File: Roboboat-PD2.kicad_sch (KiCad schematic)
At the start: 36 parts, among them J1 12V, J10 Motor, J11 Motor, J12 Motor, J13 Motor, J14 5V, J15 14.4V, J17 PGOOD TP, J18 GND TP, J19 PGOOD, J2 Bucky, J3 Jetson, J4 Motor, J5 Motor, J6 Motor, J7 Motor, J8 Motor, J9 Motor, SW1 Jumper, U1 AOZ2379QI

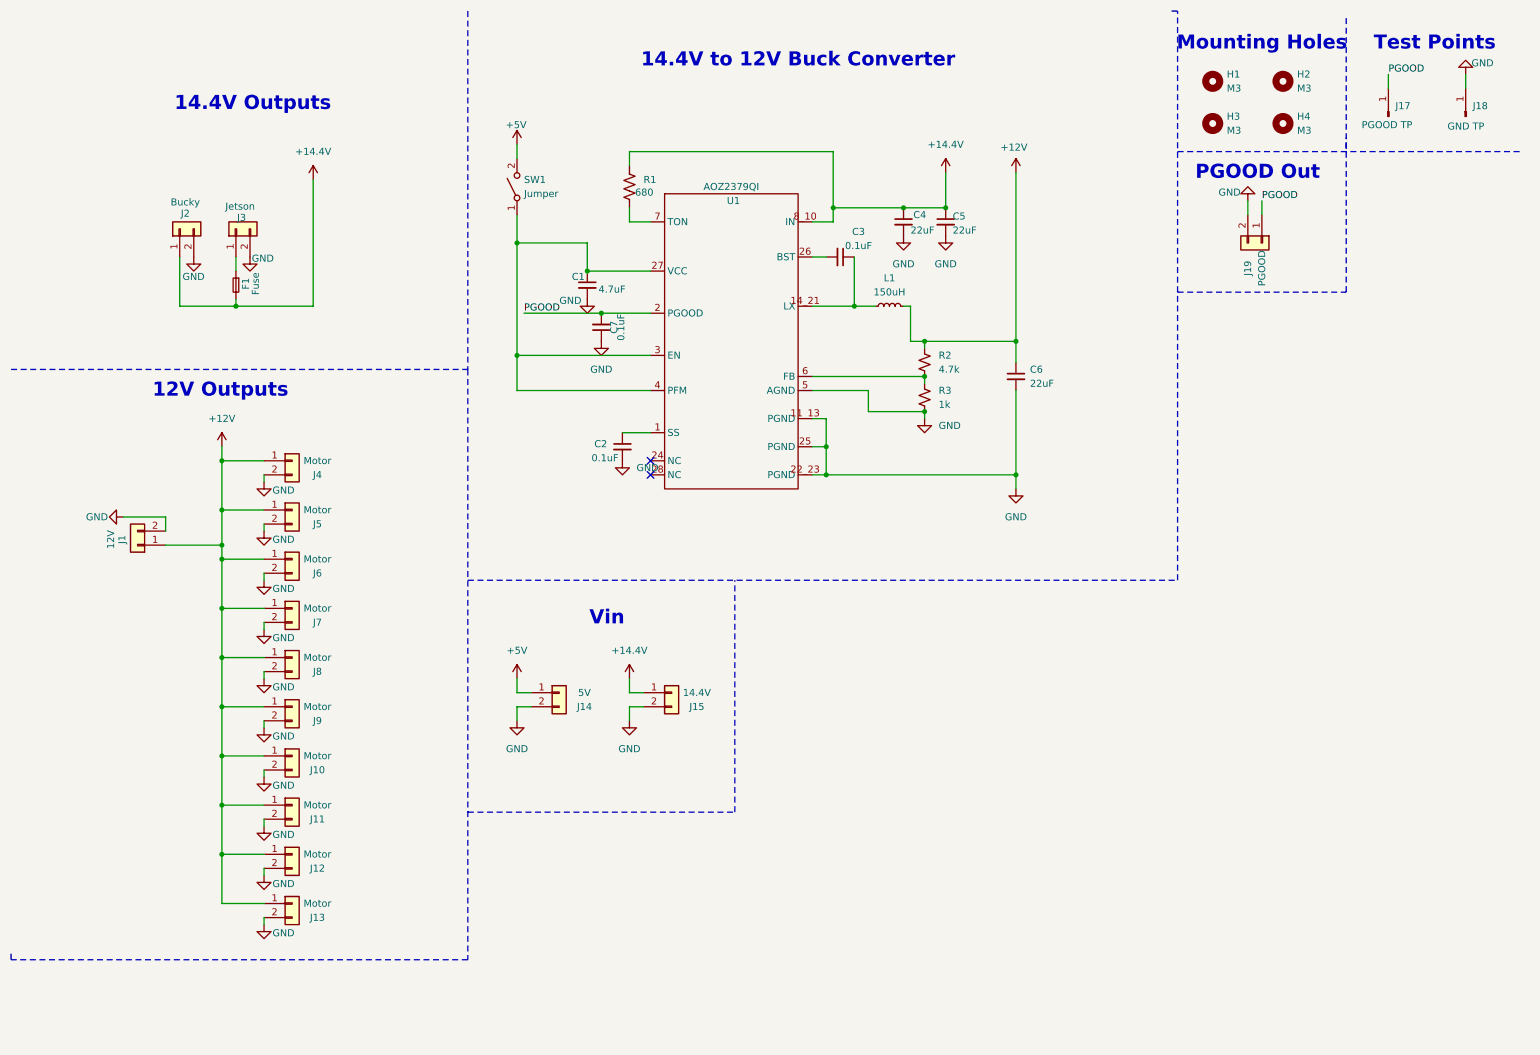
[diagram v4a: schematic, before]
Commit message: begin switch to AOZ2379QI
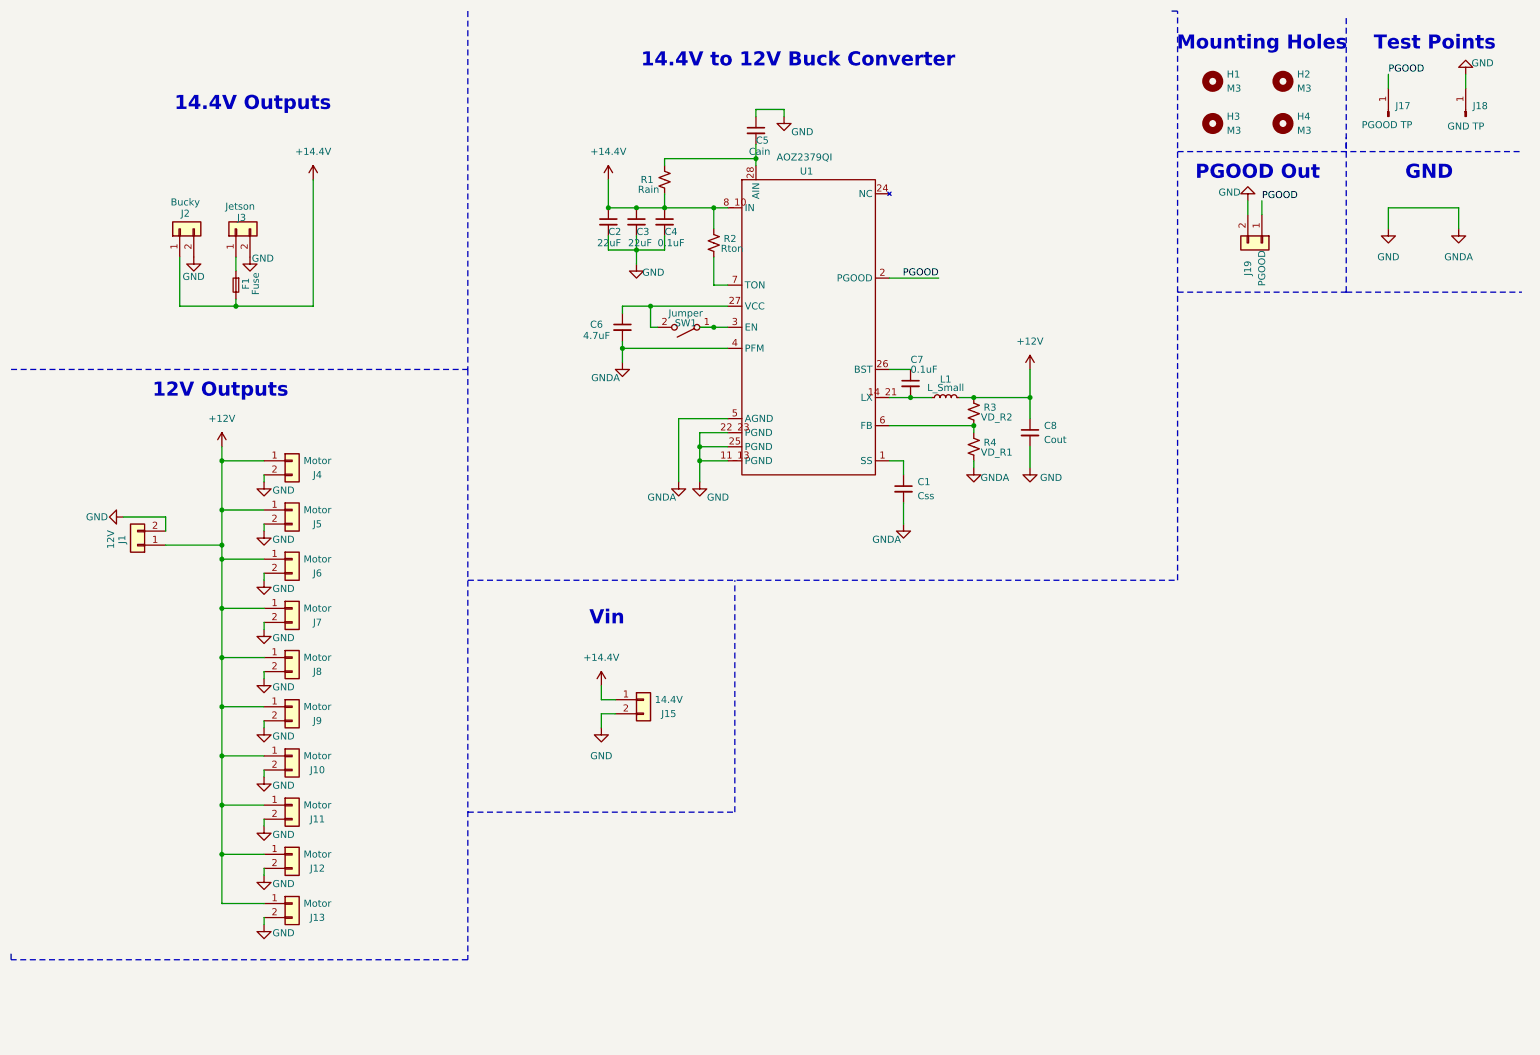
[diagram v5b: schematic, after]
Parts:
- removed J14: 5V, footprints:AMASS_XT90PW-F, symbol Connector_Generic:Conn_01x02
- removed R1: 680, Resistor_SMD:R_0805_2012Metric, symbol Device:R_US
- added C8: Cout, Capacitor_SMD:C_0805_2012Metric, symbol Device:C_Small
- added R1: Rain, Resistor_SMD:R_0805_2012Metric, symbol Device:R_Small_US
- added R4: VD_R1, Resistor_SMD:R_0805_2012Metric, symbol Device:R_Small_US
- C1: value 4.7uF -> Css; footprint footprints:CAP_CL31_SAM -> Capacitor_SMD:C_0805_2012Metric
- C2, C3: value 0.1uF -> 22uF; footprint Capacitor_SMD:C_1206_3216Metric -> Capacitor_SMD:C_0805_2012Metric
- C4: value 22uF -> 0.1uF; footprint Capacitor_SMD:C_1206_3216Metric -> Capacitor_SMD:C_0805_2012Metric
- C5: value 22uF -> Cain; footprint Capacitor_SMD:C_1206_3216Metric -> Capacitor_SMD:C_0805_2012Metric
- C6: value 22uF -> 4.7uF; footprint Capacitor_SMD:C_1206_3216Metric -> Capacitor_SMD:C_0805_2012Metric
- C7: footprint Capacitor_SMD:C_1206_3216Metric -> Capacitor_SMD:C_0805_2012Metric
- L1: value 150uH -> L_Small
- R2: value 4.7k -> Rton
- R3: value 1k -> VD_R2
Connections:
- net +12V: now also R3.1, C8.1; no longer C6.1, R2.1
- net +14.4V: now also C2.1, C3.1, R2.1, R1.2; no longer C5.1
- net GND: now also C3.2, C5.1, U1.4 (PFM), C8.2, R4.2; no longer C5.2, C7.1, R3.2
- net PGOOD: no longer C7.2
- net at U1.7 (TON): now also R2.2
- net at U1.1 (SS): now also C1.1; no longer C2.1
- net at L1.1, U1.14_21 (LX): now also C7.2; no longer C3.1
- net at U1.26 (BST): now also C7.1; no longer C3.2
- net at U1.28 (AIN): now also C5.2, R1.1
- net +5V: no longer names the net of SW1.2 (B)
- net +5V: now also C6.1, U1.27 (VCC)
- new net: R3.2, R4.1, U1.6 (FB)
- new net: SW1.1 (A), U1.3 (EN)
- no-connect marks 2 -> 0
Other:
- note added: "GND"
- moved on the sheet: J15

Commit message: rearrange schematic
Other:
- note added: "14.4V Input"
- note removed: "Vin"
- moved on the sheet: F1, H1, H2, H3, H4, J1, J10, J11, J12, J13, J15, J19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

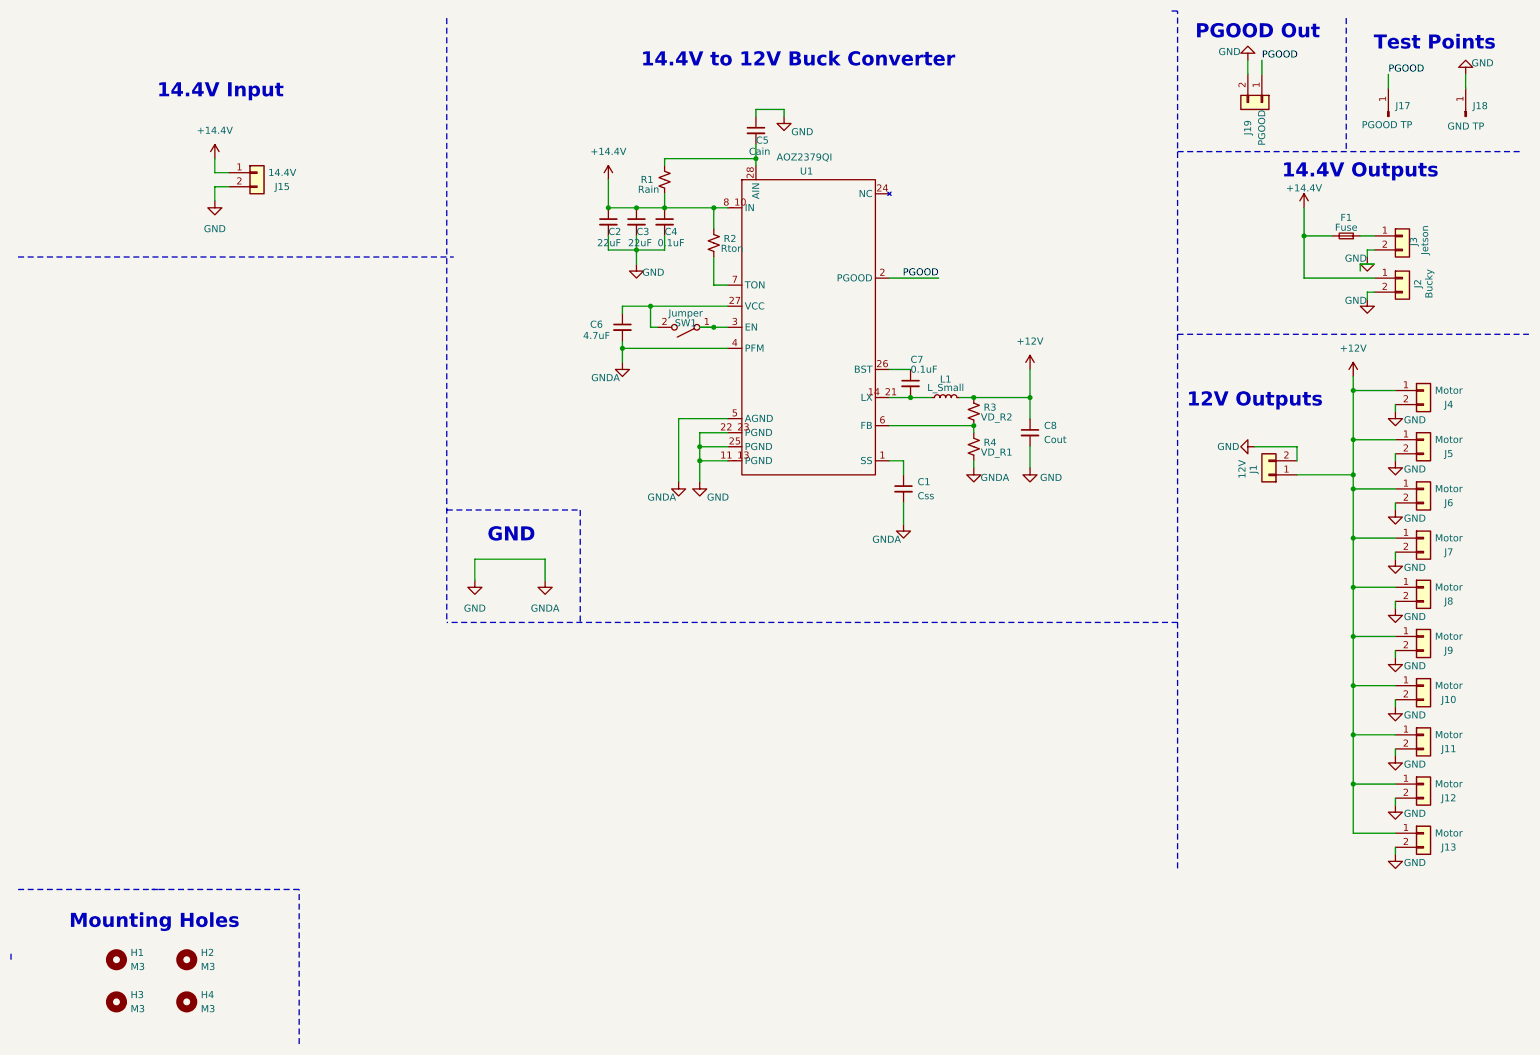
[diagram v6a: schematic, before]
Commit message: hesitant buck converter circuit values
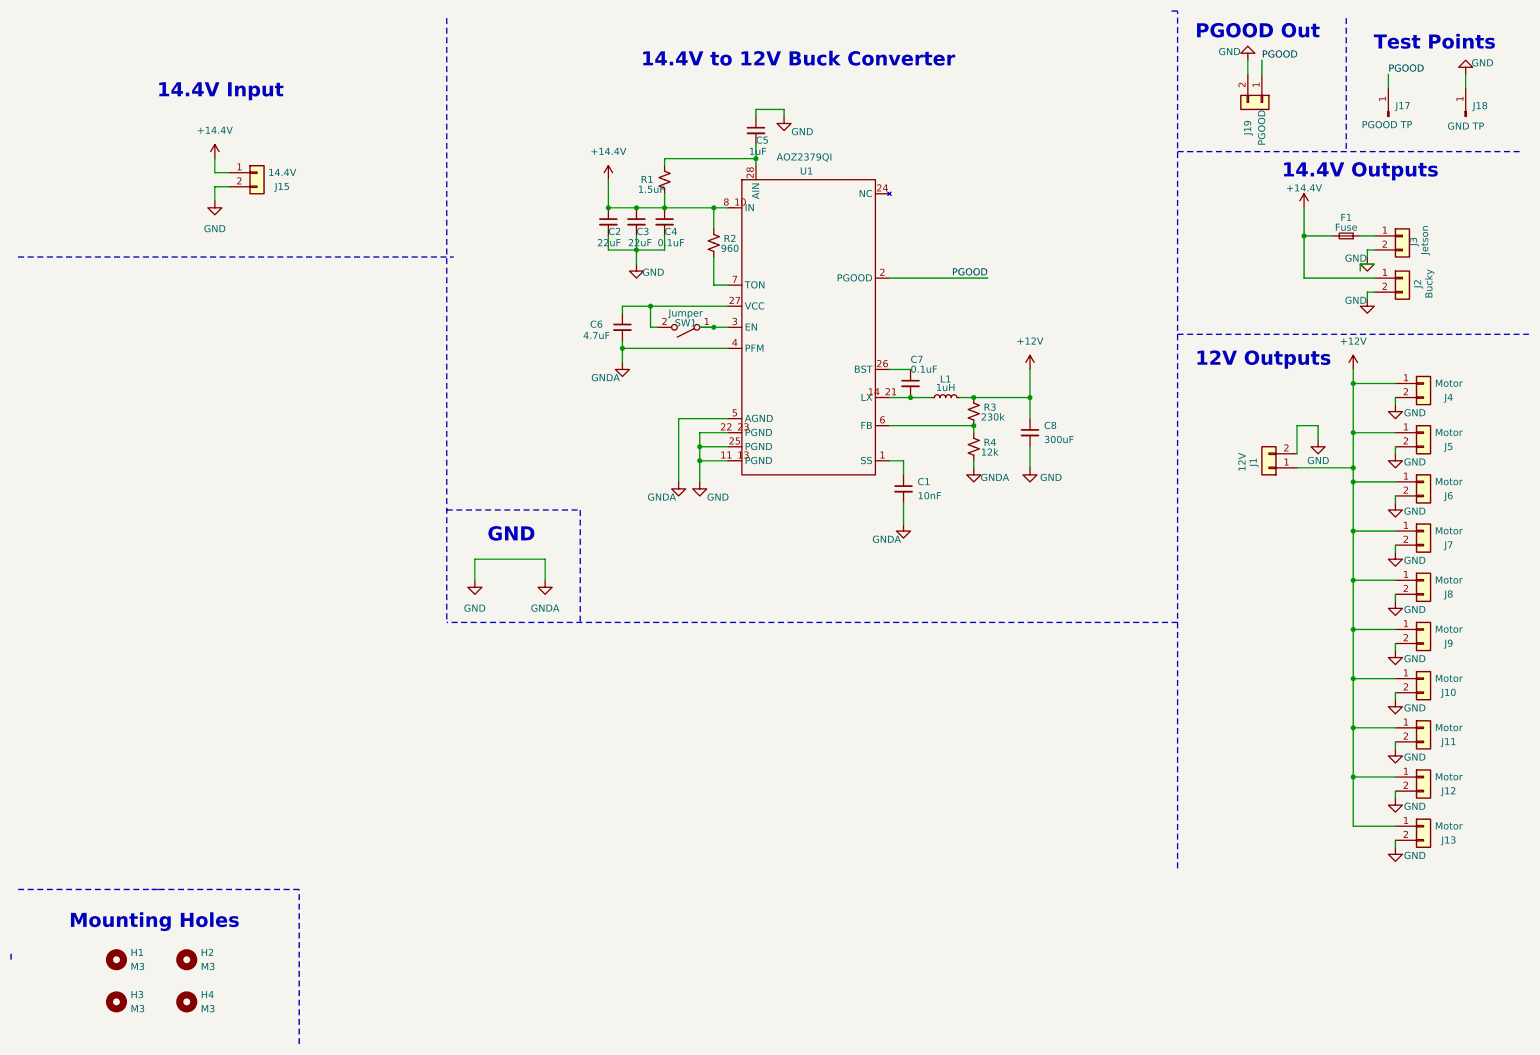
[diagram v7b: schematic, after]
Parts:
- C1: value Css -> 10nF
- C5: value Cain -> 1uF
- C8: value Cout -> 300uF
- L1: value L_Small -> 1uH
- R1: value Rain -> 1.5uF
- R2: value Rton -> 960
- R3: value VD_R2 -> 230k
- R4: value VD_R1 -> 12k
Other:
- moved on the sheet: J1, J10, J11, J12, J13, J4, J5, J6, J7, J8, J9

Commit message: correct XT-90 footprints
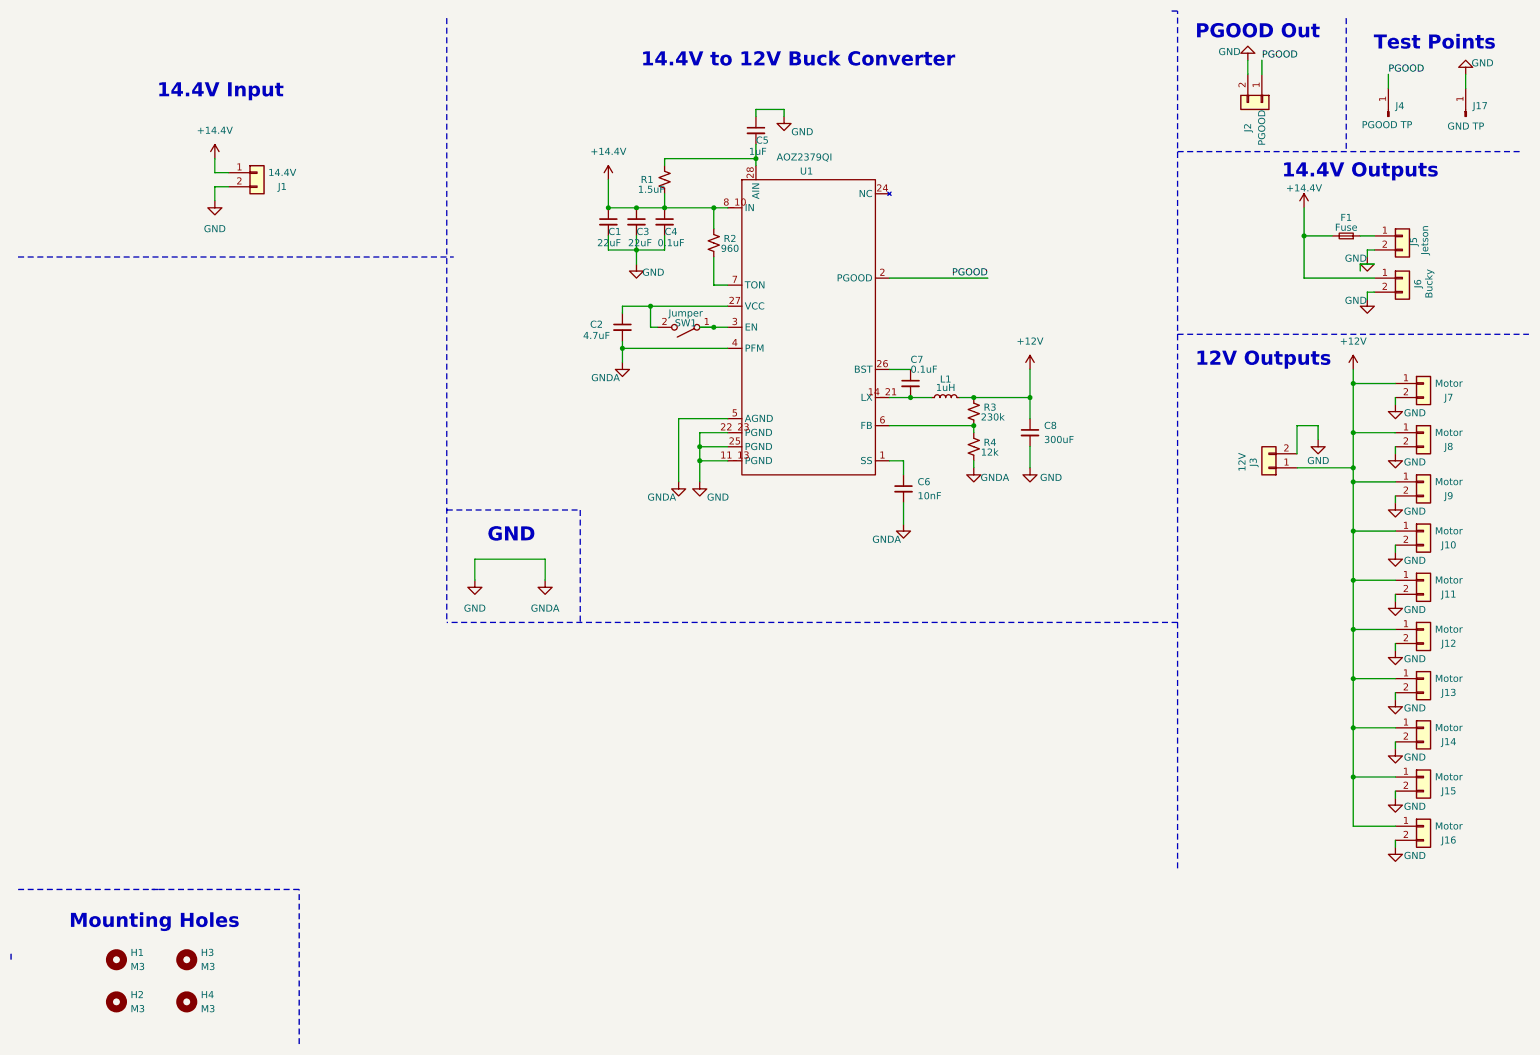
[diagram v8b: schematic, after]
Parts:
- J1: renamed from J15; footprint footprints:AMASS_XT90PW-F -> footprints:XT90_V
- J3: renamed from J1; footprint footprints:AMASS_XT90PW-F -> footprints:XT90_V
- J5: renamed from J3; footprint footprints:AMASS_XT90PW-F -> footprints:XT90_V
- J6: renamed from J2; footprint footprints:AMASS_XT90PW-F -> footprints:XT90_V
- renumbered C2 to C1, C6 to C2, C1 to C6, H3 to H2, H2 to H3, J7 to J10, J8 to J11, J9 to J12, J10 to J13, J11 to J14, J12 to J15, J13 to J16, J18 to J17, J19 to J2, J17 to J4, J4 to J7, J5 to J8, J6 to J9
